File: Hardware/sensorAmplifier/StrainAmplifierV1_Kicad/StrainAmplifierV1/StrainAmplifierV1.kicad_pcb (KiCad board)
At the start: 2 copper layers, 23 x 13.5 mm, 13 parts, among them U1 INA333AIDGKR, U2 TLV9061SQDBVRQ1

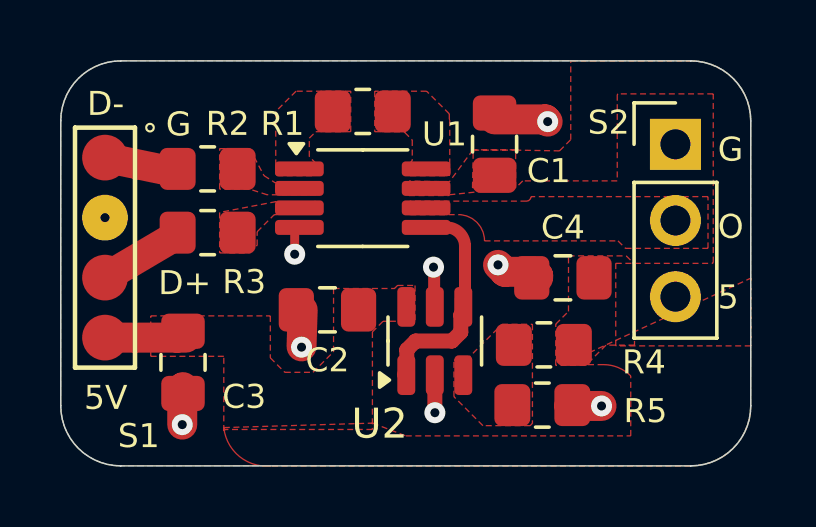
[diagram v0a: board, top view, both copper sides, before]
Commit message: - Redo buck converter calculations - Maybe stimulate it. - Choose components for RC mosfet circuit - Verify MOSFET calculations - tried and changed PMOS type - Check fuse selection. Accounting for BUCK CONVERTER efficiency - Replace ZENER DIODES component
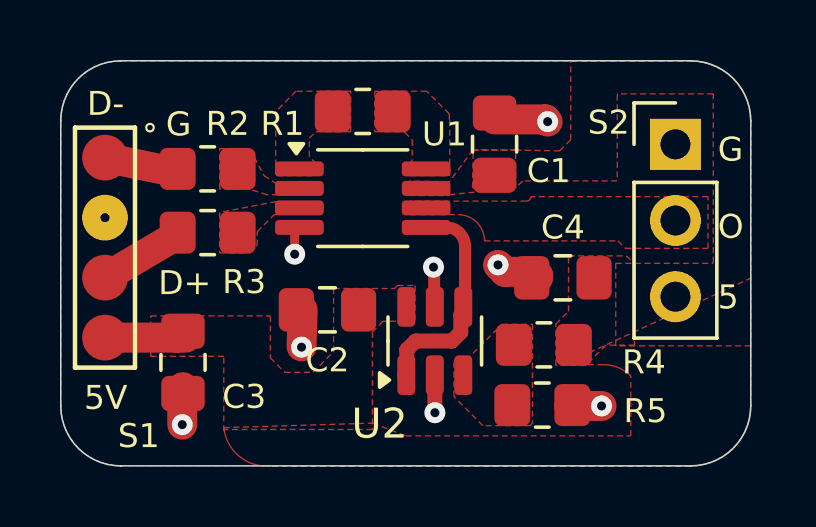
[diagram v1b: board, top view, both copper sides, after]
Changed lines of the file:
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@@
 	)
 	(gr_line
-		(start 139.0011 98.2536)
-		(end 158.0011 98.2536)
+		(start 138.99049 98.24941)
+		(end 157.99049 98.24941)
 		(stroke
 			(width 0.05)
